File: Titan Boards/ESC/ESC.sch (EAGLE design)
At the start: 105 parts, among them IC1 7425D, IC2 74AHC1G08DBV, Q1 5.8A/30V/35mΩ, Q2 5.8A/30V/35mΩ, Q3 5.8A/30V/35mΩ, Q4 5.8A/30V/35mΩ, Q5 5.8A/30V/35mΩ, Q6 5.8A/30V/35mΩ, Q7 5.8A/30V/35mΩ, Q8 5.8A/30V/35mΩ

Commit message: FInal ESC after review
See summary
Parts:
- renumbered FUSE_1 to F1, FUSE_2 to F2, FUSE_3 to F3, FUSE_4 to F4, FUSE_5 to F5, FUSE_6 to F6, FUSE_7 to F7, FUSE_8 to F8
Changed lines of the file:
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@@
 <part name="2-PIN_3" library="Screw_Terminals" deviceset="1711725" device=""/>
 <part name="2-PIN_2" library="Screw_Terminals" deviceset="1711725" device=""/>
-<part name="FUSE_5" library="1206 fuse holder" deviceset="1206FUSEHOLDER" device=""/>
-<part name="FUSE_6" library="1206 fuse holder" deviceset="1206FUSEHOLDER" device=""/>
-<part name="FUSE_7" library="1206 fuse holder" deviceset="1206FUSEHOLDER" device=""/>
-<part name="FUSE_8" library="1206 fuse holder" deviceset="1206FUSEHOLDER" device=""/>
-<part name="FUSE_4" library="1206 fuse holder" deviceset="1206FUSEHOLDER" device=""/>
-<part name="FUSE_3" library="1206 fuse holder" deviceset="1206FUSEHOLDER" device=""/>
-<part name="FUSE_2" library="1206 fuse holder" deviceset="1206FUSEHOLDER" device=""/>
-<part name="FUSE_1" library="1206 fuse holder" deviceset="1206FUSEHOLDER" device=""/>
+<part name="F5" library="1206 fuse holder" deviceset="1206FUSEHOLDER" device=""/>
+<part name="F6" library="1206 fuse holder" deviceset="1206FUSEHOLDER" device=""/>
+<part name="F7" library="1206 fuse holder" deviceset="1206FUSEHOLDER" device=""/>
+<part name="F8" library="1206 fuse holder" deviceset="1206FUSEHOLDER" device=""/>
+<part name="F4" library="1206 fuse holder" deviceset="1206FUSEHOLDER" device=""/>
+<part name="F3" library="1206 fuse holder" deviceset="1206FUSEHOLDER" device=""/>
+<part name="F2" library="1206 fuse holder" deviceset="1206FUSEHOLDER" device=""/>
+<part name="F1" library="1206 fuse holder" deviceset="1206FUSEHOLDER" device=""/>
 <part name="FRAME3" library="frames" library_urn="urn:adsk.eagle:library:229" deviceset="A3L-LOC" device=""/>
 <part name="CS_1" library="ACS722" deviceset="ACS722" device=""/>
@@
 <instance part="2-PIN_3" gate="G$1" x="236.22" y="106.68" smashed="yes"/>
 <instance part="2-PIN_2" gate="G$1" x="236.22" y="121.92" smashed="yes"/>
-<instance part="FUSE_5" gate="G$1" x="284.48" y="144.78" smashed="yes"/>
-<instance part="FUSE_6" gate="G$1" x="284.48" y="129.54" smashed="yes"/>
-<instance part="FUSE_7" gate="G$1" x="284.48" y="114.3" smashed="yes"/>
-<instance part="FUSE_8" gate="G$1" x="284.48" y="99.06" smashed="yes"/>
-<instance part="FUSE_4" gate="G$1" x="200.66" y="93.98" smashed="yes"/>
-<instance part="FUSE_3" gate="G$1" x="200.66" y="109.22" smashed="yes"/>
-<instance part="FUSE_2" gate="G$1" x="200.66" y="124.46" smashed="yes"/>
-<instance part="FUSE_1" gate="G$1" x="200.66" y="139.7" smashed="yes"/>
+<instance part="F5" gate="G$1" x="284.48" y="144.78" smashed="yes"/>
+<instance part="F6" gate="G$1" x="284.48" y="129.54" smashed="yes"/>
+<instance part="F7" gate="G$1" x="284.48" y="114.3" smashed="yes"/>
+<instance part="F8" gate="G$1" x="284.48" y="99.06" smashed="yes"/>
+<instance part="F4" gate="G$1" x="200.66" y="93.98" smashed="yes"/>
+<instance part="F3" gate="G$1" x="200.66" y="109.22" smashed="yes"/>
+<instance part="F2" gate="G$1" x="200.66" y="124.46" smashed="yes"/>
+<instance part="F1" gate="G$1" x="200.66" y="139.7" smashed="yes"/>
 <instance part="+3V4" gate="G$1" x="124.46" y="96.52" smashed="yes" rot="R180">
 <attribute name="VALUE" x="127" y="101.6" size="1.778" layer="96" rot="R270"/>
@@
 <net name="FUSE_1_TRIGGER" class="0">
 <segment>
-<pinref part="FUSE_1" gate="G$1" pin="P$2"/>
+<pinref part="F1" gate="G$1" pin="P$2"/>
 <pinref part="2-PIN_1" gate="G$1" pin="BLACK"/>
 <wire x1="213.36" y1="139.7" x2="215.9" y2="139.7" width="0.1524" layer="91"/>
@@
 <segment>
 <pinref part="2-PIN_5" gate="G$1" pin="BLACK"/>
-<pinref part="FUSE_5" gate="G$1" pin="P$1"/>
+<pinref part="F5" gate="G$1" pin="P$1"/>
 <wire x1="259.08" y1="144.78" x2="269.24" y2="144.78" width="0.1524" layer="91"/>
 <wire x1="269.24" y1="144.78" x2="271.78" y2="144.78" width="0.1524" layer="91"/>
@@
 <net name="FUSE_6_TRIGGER" class="0">
 <segment>
-<pinref part="FUSE_6" gate="G$1" pin="P$1"/>
+<pinref part="F6" gate="G$1" pin="P$1"/>
 <pinref part="2-PIN_6" gate="G$1" pin="BLACK"/>
 <wire x1="271.78" y1="129.54" x2="269.24" y2="129.54" width="0.1524" layer="91"/>
@@
 <segment>
 <pinref part="2-PIN_7" gate="G$1" pin="BLACK"/>
-<pinref part="FUSE_7" gate="G$1" pin="P$1"/>
+<pinref part="F7" gate="G$1" pin="P$1"/>
 <wire x1="259.08" y1="114.3" x2="269.24" y2="114.3" width="0.1524" layer="91"/>
 <wire x1="269.24" y1="114.3" x2="271.78" y2="114.3" width="0.1524" layer="91"/>
@@
 <segment>
 <pinref part="2-PIN_8" gate="G$1" pin="BLACK"/>
-<pinref part="FUSE_8" gate="G$1" pin="P$1"/>
+<pinref part="F8" gate="G$1" pin="P$1"/>
 <wire x1="259.08" y1="99.06" x2="269.24" y2="99.06" width="0.1524" layer="91"/>
 <wire x1="269.24" y1="99.06" x2="271.78" y2="99.06" width="0.1524" layer="91"/>
@@
 <segment>
 <pinref part="2-PIN_4" gate="G$1" pin="BLACK"/>
-<pinref part="FUSE_4" gate="G$1" pin="P$2"/>
+<pinref part="F4" gate="G$1" pin="P$2"/>
 <wire x1="223.52" y1="93.98" x2="215.9" y2="93.98" width="0.1524" layer="91"/>
 <wire x1="215.9" y1="93.98" x2="213.36" y2="93.98" width="0.1524" layer="91"/>
@@
 <segment>
 <pinref part="2-PIN_3" gate="G$1" pin="BLACK"/>
-<pinref part="FUSE_3" gate="G$1" pin="P$2"/>
+<pinref part="F3" gate="G$1" pin="P$2"/>
 <wire x1="223.52" y1="109.22" x2="215.9" y2="109.22" width="0.1524" layer="91"/>
 <wire x1="215.9" y1="109.22" x2="213.36" y2="109.22" width="0.1524" layer="91"/>
@@
 <segment>
 <pinref part="2-PIN_2" gate="G$1" pin="BLACK"/>
-<pinref part="FUSE_2" gate="G$1" pin="P$2"/>
+<pinref part="F2" gate="G$1" pin="P$2"/>
 <wire x1="223.52" y1="124.46" x2="215.9" y2="124.46" width="0.1524" layer="91"/>
 <wire x1="215.9" y1="124.46" x2="213.36" y2="124.46" width="0.1524" layer="91"/>
@@
 <net name="FUSED_1" class="0">
 <segment>
-<pinref part="FUSE_1" gate="G$1" pin="P$1"/>
+<pinref part="F1" gate="G$1" pin="P$1"/>
 <wire x1="187.96" y1="139.7" x2="185.42" y2="139.7" width="0.1524" layer="91"/>
 <label x="185.42" y="139.7" size="1.27" layer="95" rot="R180" xref="yes"/>
@@
 <net name="FUSED_2" class="0">
 <segment>
-<pinref part="FUSE_2" gate="G$1" pin="P$1"/>
+<pinref part="F2" gate="G$1" pin="P$1"/>
 <wire x1="187.96" y1="124.46" x2="185.42" y2="124.46" width="0.1524" layer="91"/>
 <label x="185.42" y="124.46" size="1.27" layer="95" rot="R180" xref="yes"/>
@@
 <net name="FUSED_3" class="0">
 <segment>
-<pinref part="FUSE_3" gate="G$1" pin="P$1"/>
+<pinref part="F3" gate="G$1" pin="P$1"/>
 <wire x1="187.96" y1="109.22" x2="185.42" y2="109.22" width="0.1524" layer="91"/>
 <label x="185.42" y="109.22" size="1.27" layer="95" rot="R180" xref="yes"/>
@@
 <net name="FUSED_4" class="0">
 <segment>
-<pinref part="FUSE_4" gate="G$1" pin="P$1"/>
+<pinref part="F4" gate="G$1" pin="P$1"/>
 <wire x1="187.96" y1="93.98" x2="185.42" y2="93.98" width="0.1524" layer="91"/>
 <label x="185.42" y="93.98" size="1.27" layer="95" rot="R180" xref="yes"/>
@@
 <net name="FUSED_8" class="0">
 <segment>
-<pinref part="FUSE_8" gate="G$1" pin="P$2"/>
+<pinref part="F8" gate="G$1" pin="P$2"/>
 <wire x1="297.18" y1="99.06" x2="299.72" y2="99.06" width="0.1524" layer="91"/>
 <label x="299.72" y="99.06" size="1.27" layer="95" xref="yes"/>
@@
 <net name="FUSED_7" class="0">
 <segment>
-<pinref part="FUSE_7" gate="G$1" pin="P$2"/>
+<pinref part="F7" gate="G$1" pin="P$2"/>
 <wire x1="297.18" y1="114.3" x2="299.72" y2="114.3" width="0.1524" layer="91"/>
 <label x="299.72" y="114.3" size="1.27" layer="95" xref="yes"/>
@@
 <net name="FUSED_6" class="0">
 <segment>
-<pinref part="FUSE_6" gate="G$1" pin="P$2"/>
+<pinref part="F6" gate="G$1" pin="P$2"/>
 <wire x1="297.18" y1="129.54" x2="299.72" y2="129.54" width="0.1524" layer="91"/>
 <label x="299.72" y="129.54" size="1.27" layer="95" xref="yes"/>
@@
 <net name="FUSED_5" class="0">
 <segment>
-<pinref part="FUSE_5" gate="G$1" pin="P$2"/>
+<pinref part="F5" gate="G$1" pin="P$2"/>
 <wire x1="297.18" y1="144.78" x2="299.72" y2="144.78" width="0.1524" layer="91"/>
 <label x="299.72" y="144.78" size="1.27" layer="95" xref="yes"/>
@@
 <pinref part="Q1" gate="NMOS" pin="S"/>
 <wire x1="53.34" y1="76.2" x2="53.34" y2="63.5" width="0.1524" layer="91"/>
+<junction x="45.72" y="63.5"/>
 </segment>
 <segment>
@@
 <pinref part="Q2" gate="NMOS" pin="S"/>
 <wire x1="78.74" y1="76.2" x2="78.74" y2="63.5" width="0.1524" layer="91"/>
+<junction x="71.12" y="63.5"/>
 </segment>
 <segment>
@@
 <pinref part="Q3" gate="NMOS" pin="S"/>
 <wire x1="101.6" y1="76.2" x2="101.6" y2="63.5" width="0.1524" layer="91"/>
+<junction x="93.98" y="63.5"/>
 </segment>
 <segment>
@@
 <pinref part="Q4" gate="NMOS" pin="S"/>
 <wire x1="127" y1="76.2" x2="127" y2="63.5" width="0.1524" layer="91"/>
+<junction x="119.38" y="63.5"/>
 </segment>
 <segment>
@@
 <pinref part="Q5" gate="NMOS" pin="S"/>
 <wire x1="152.4" y1="76.2" x2="152.4" y2="63.5" width="0.1524" layer="91"/>
+<junction x="144.78" y="63.5"/>
 </segment>
 <segment>
@@
 <pinref part="Q6" gate="NMOS" pin="S"/>
 <wire x1="177.8" y1="76.2" x2="177.8" y2="63.5" width="0.1524" layer="91"/>
+<junction x="170.18" y="63.5"/>
 </segment>
 <segment>
@@
 <pinref part="Q7" gate="NMOS" pin="S"/>
 <wire x1="205.74" y1="76.2" x2="205.74" y2="63.5" width="0.1524" layer="91"/>
+<junction x="198.12" y="63.5"/>
 </segment>
 <segment>
@@
 <pinref part="Q8" gate="NMOS" pin="S"/>
 <wire x1="233.68" y1="76.2" x2="233.68" y2="63.5" width="0.1524" layer="91"/>
+<junction x="226.06" y="63.5"/>
 </segment>
 <segment>

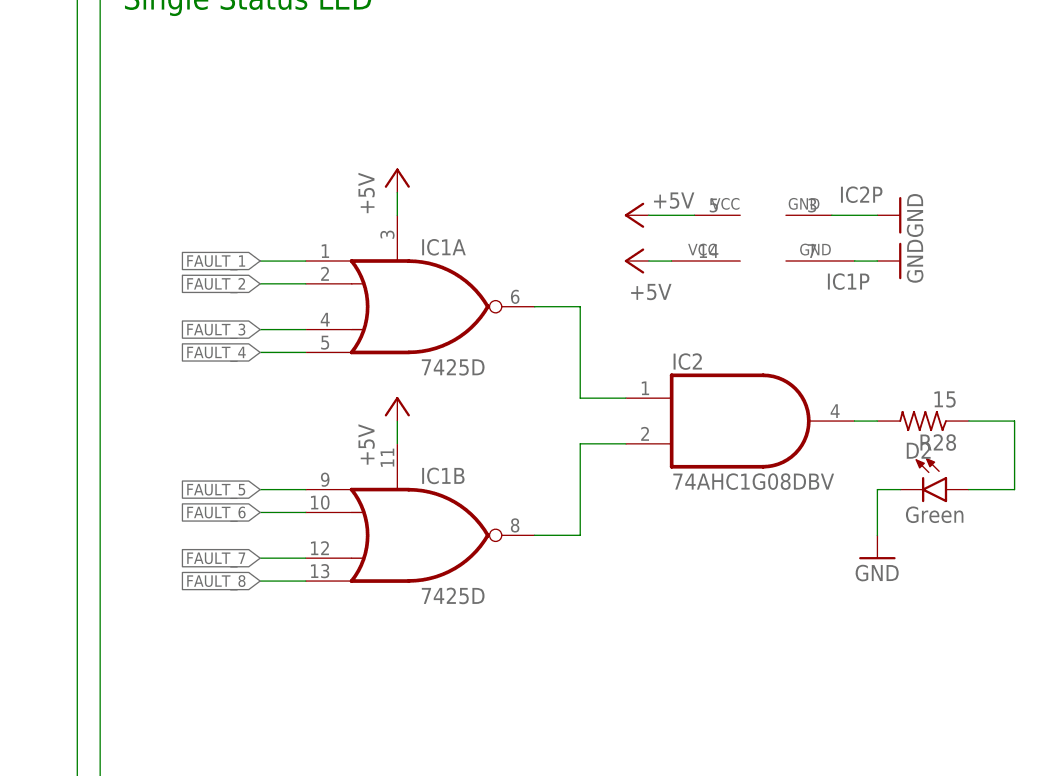
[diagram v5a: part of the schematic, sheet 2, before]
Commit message: final commit of Titan ESC
slight cosmetic changes to ESC board
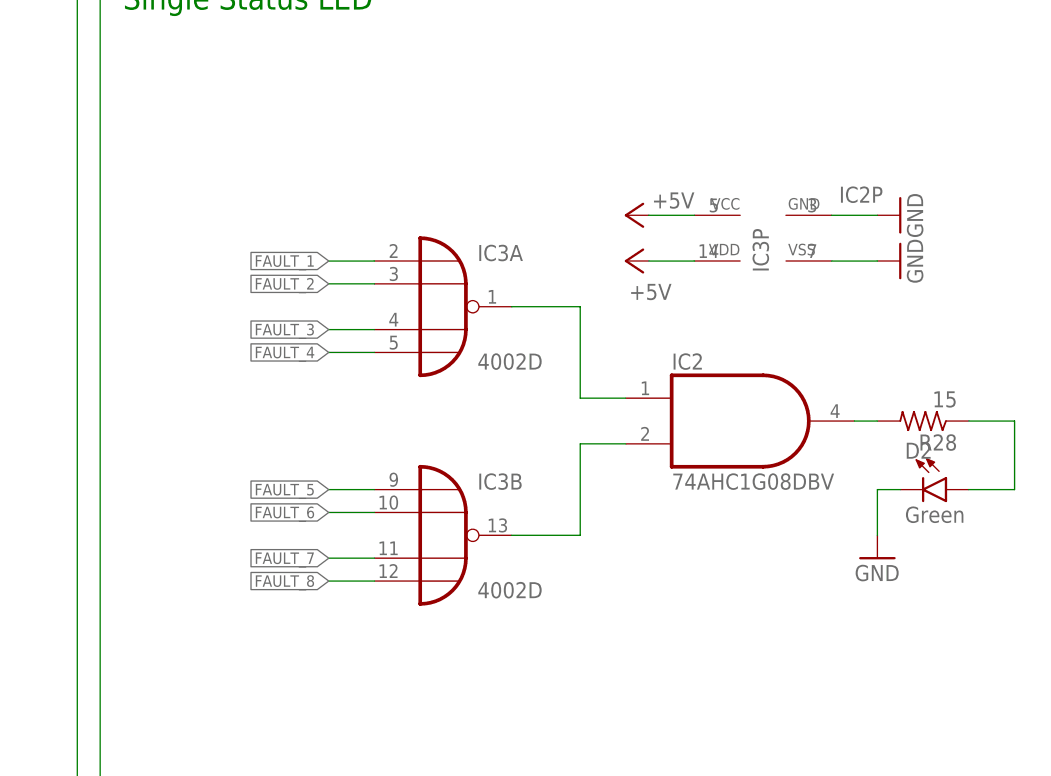
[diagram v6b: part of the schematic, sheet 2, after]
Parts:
- removed IC1: 7425D, 74xx-us:7425D
- added IC3: 4002D, 40xx:4002D
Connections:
- net +5V: now also IC3P.VDD; no longer IC1A.G, IC1B.G, IC1P.VCC
- net FAULT_1: now also IC3A.I0; no longer IC1A.I0
- net FAULT_2: now also IC3A.I1; no longer IC1A.I1
- net FAULT_3: now also IC3A.I2; no longer IC1A.I2
- net FAULT_4: now also IC3A.I3; no longer IC1A.I3
- net FAULT_5: now also IC3B.I0; no longer IC1B.I0
- net FAULT_6: now also IC3B.I1; no longer IC1B.I1
- net FAULT_7: now also IC3B.I2; no longer IC1B.I2
- net FAULT_8: now also IC3B.I3; no longer IC1B.I3
- net GND: now also IC3P.VSS; no longer IC1P.GND
- net NOR_1_OUT: now also IC3A.O; no longer IC1A.O
- net NOR_2_OUT: now also IC3B.O; no longer IC1B.O
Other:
- note added: "2 Circuit 4 Input NOR Gate"
- note added: "2-input AND gate: SN74LVC1G08 https://www.digikey.com/en/products/detail/texas-instruments/SN74LVC1G08DBVR/385718 https://www.ti.com/lit/ds/symlink/sn74lvc1g08.pdf? HQS=dis-dk-null-digikeymode-dsf-pf-null-wwe&ts=1611067529349"
- note added: "Fuse Fault Circuit simulated in Multisim to ensure functionality."
- note added: "Fuses: Eaton 3216FF 10A 24V https://www.digikey.com/en/products/detail/littelfuse-inc/0451010-MRL/700832 https://www.littelfuse.com/~/media/electronics/datasheets/fuses/ littelfuse_fuse_451_453_datasheet.pdf.pdf"
- note added: "NOR Gate: CD74HC4002M https://www.digikey.com/en/products/detail/texas-instruments/CD74HC4002M/1507041 https://www.ti.com/lit/ds/symlink/cd74hc4002.pdf? HQS=dis-dk-null-digikeymode-dsf-pf-null-wwe&ts=1611114244711"
- note added: "PWM Connectors: 1x4 Pin Male Breakaway Header Pins https://www.digikey.com/en/products/detail/molex/0901200124/760789 https://www.molex.com/pdm_docs/sd/901200124_sd.pdf"
- note removed: "Fuse Fault Circuit simulated in Multisim to ensure functionality. Fault circuit uses an "OR" gate to turn off the single status LED."
- note removed: "Fuses: Eaton 3216FF 10A 24V https://www.digikey.com/product-detail/en/ eaton-electronics-division/TR-3216FF10-R/283-5280-1-ND/9644851 https://www.eaton.com/content/dam/eaton/products/electronic-components/resources/data-sheet/ eaton-3216ff-surface-mount-fuse-data-sheet.pdf"
- note removed: "PWM Connectors: 1X3 Male Breakaway Header Pins https://www.digikey.com/product-detail/en/molex/0901200123/WM8073-ND/760788 https://www.molex.com/pdm_docs/sd/901200123_sd.pdf"
- note removed: "Single Status LED Transistor: BJT 2N2222 https://www.digikey.com/product-detail/en/diodes-incorporated/ MMBT2222A-7-F/MMBT2222A-FDICT-ND/815723 https://www.diodes.com/assets/Datasheets/ds30041.pdf"

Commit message: ESC Updates + library additions
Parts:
- 2-PIN_1, 2-PIN_2, 2-PIN_3, 2-PIN_4, 2-PIN_5, 2-PIN_6, 2-PIN_7, 2-PIN_8: value 1711725 -> 1755736; device Screw_Terminals:1711725 -> Screw_Terminals:1755736
- 3-PIN_1, 3-PIN_2, 3-PIN_3, 3-PIN_4, 3-PIN_5, 3-PIN_6, 3-PIN_7, 3-PIN_8: value 1711738 -> 1755749; device Screw_Terminals:1711738 -> Screw_Terminals:1755749
- R12, R15, R18, R19, R22, R25, R6, R9: value 28 -> 150
- R28: value 15 -> 91
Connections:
- removed net N$13: 24-PIN_CONNECTOR.8,WHITE, 3-PIN_5.WHITE
- removed net N$15: 24-PIN_CONNECTOR.8,BLUE, 3-PIN_5.BLUE
- removed net N$16: 24-PIN_CONNECTOR.6,WHITE, 3-PIN_6.WHITE
- removed net N$18: 24-PIN_CONNECTOR.6,BLUE, 3-PIN_6.BLUE
- removed net N$2 (its old number): 24-PIN_CONNECTOR.1,GREEN, 3-PIN_4.GREEN
- removed net N$23 (its old number): 24-PIN_CONNECTOR.2,BLUE, 3-PIN_8.BLUE
- removed net N$4 (its old number): 24-PIN_CONNECTOR.3,WHITE, 3-PIN_3.WHITE
- removed net N$5 (its old number): 24-PIN_CONNECTOR.3,GREEN, 3-PIN_3.GREEN
- removed net N$6 (its old number): 24-PIN_CONNECTOR.3,BLUE, 3-PIN_3.BLUE
- removed net N$8 (its old number): 24-PIN_CONNECTOR.5,GREEN, 3-PIN_2.GREEN
- new net N$22: 24-PIN_CONNECTOR.2,BLUE, 3-PIN_8.WHITE
- net N$1: now also 24-PIN_CONNECTOR.8,BLUE, 3-PIN_5.WHITE; no longer 24-PIN_CONNECTOR.1,BLUE, 3-PIN_4.BLUE
- net N$19: now also 24-PIN_CONNECTOR.4,WHITE; no longer 24-PIN_CONNECTOR.4,BLUE
- net N$21: now also 24-PIN_CONNECTOR.4,BLUE; no longer 24-PIN_CONNECTOR.4,WHITE
- net N$24: now also 3-PIN_8.BLUE; no longer 3-PIN_8.WHITE
- net N$3: now also 24-PIN_CONNECTOR.8,WHITE, 3-PIN_5.BLUE; no longer 24-PIN_CONNECTOR.1,WHITE, 3-PIN_4.WHITE
- net N$7: now also 24-PIN_CONNECTOR.6,BLUE, 3-PIN_6.WHITE; no longer 24-PIN_CONNECTOR.5,BLUE, 3-PIN_2.BLUE
- net N$9: now also 24-PIN_CONNECTOR.6,WHITE, 3-PIN_6.BLUE; no longer 24-PIN_CONNECTOR.5,WHITE, 3-PIN_2.WHITE
